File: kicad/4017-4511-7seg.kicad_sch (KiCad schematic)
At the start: 15 parts, among them U7 4017, U8 4511, U9 D168K

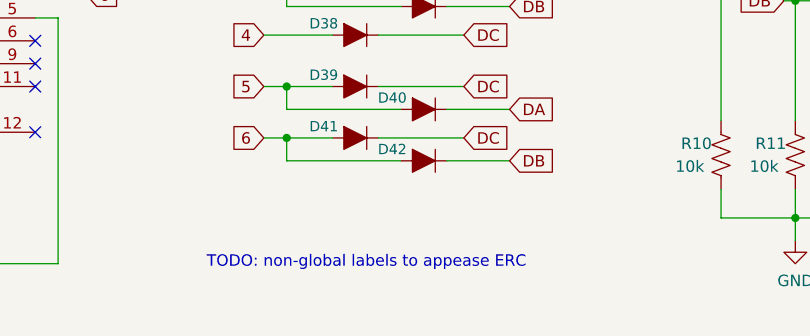
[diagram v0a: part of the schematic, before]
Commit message: Note BOM effects in different implementations
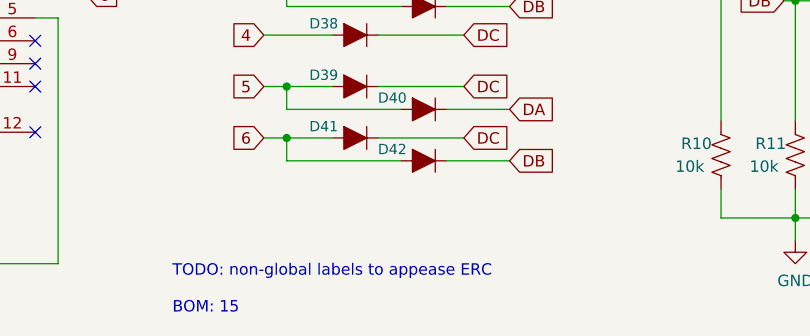
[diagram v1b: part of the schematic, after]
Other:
- note added: "TODO: non-global labels to appease ERC BOM: 15"
- note removed: "TODO: non-global labels to appease ERC"
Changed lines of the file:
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@@
     (stroke (width 0) (type default) (color 0 0 0 0))
   )
-  (text "TODO: non-global labels to appease ERC" (at 108.585 125.095 0)
+  (text "TODO: non-global labels to appease ERC\n\nBOM: 15" (at 104.775 130.175 0)
     (effects (font (size 1.27 1.27)) (justify left bottom))
   )

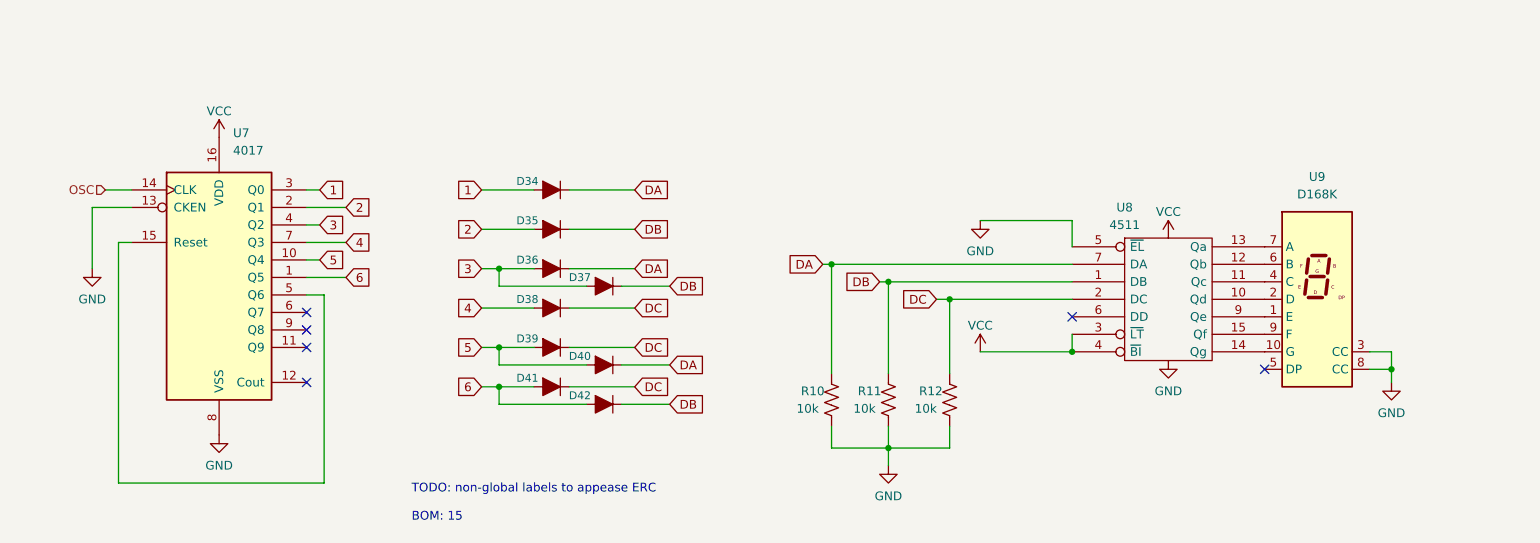
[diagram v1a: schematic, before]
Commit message: Hmmm, may need resistors for LED driver ICs
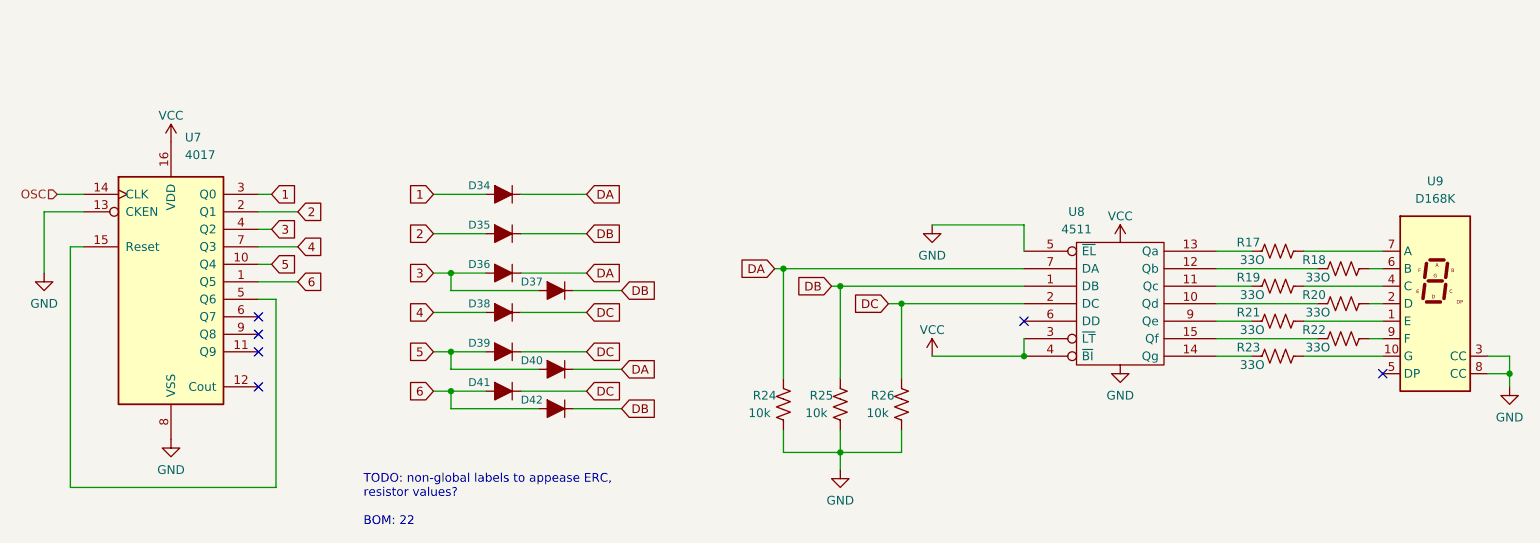
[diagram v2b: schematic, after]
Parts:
- added R17, R18, R19, R20, R21, R22, R23: 33O, Resistor_THT:R_Axial_DIN0204_L3.6mm_D1.6mm_P7.62mm_Horizontal, symbol Device:R_US
- renumbered R10 to R24, R11 to R25, R12 to R26
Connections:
- net at U8.10 (Qd): now also R20.1; no longer U9.2 (D)
- net at U8.11 (Qc): now also R19.1; no longer U9.4 (C)
- net at U8.12 (Qb): now also R18.1; no longer U9.6 (B)
- net at U8.13 (Qa): now also R17.1; no longer U9.7 (A)
- net at U8.14 (Qg): now also R23.1; no longer U9.10 (G)
- net at U8.15 (Qf): now also R22.1; no longer U9.9 (F)
- net at U8.9 (Qe): now also R21.1; no longer U9.1 (E)
- new net: R22.2, U9.9 (F)
- new net: R21.2, U9.1 (E)
- new net: R23.2, U9.10 (G)
- new net: R20.2, U9.2 (D)
- new net: R19.2, U9.4 (C)
- new net: R18.2, U9.6 (B)
- new net: R17.2, U9.7 (A)
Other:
- note added: "TODO: non-global labels to appease ERC, resistor values? BOM: 22"
- note removed: "TODO: non-global labels to appease ERC BOM: 15"
- moved on the sheet: D34, D35, D36, D37, D38, D39, D40, D41, D42, R24, R25, R26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

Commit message: TODO: fix 7seg footprint
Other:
- note added: "TODO: fix footprint! 10 A 9 B 7 C 5 D 4 E 2 F 1 G 6 DP 3 COM 8 COM"
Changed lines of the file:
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@@
     (stroke (width 0) (type default) (color 0 0 0 0))
+  )
+  (text "TODO: fix footprint!\n\n10 A\n9  B\n7  C\n5  D\n4  E\n2  F\n1  G\n\n6  DP\n3  COM\n8  COM"
+    (at 234.95 83.185 0)
+    (effects (font (size 1.27 1.27)) (justify left bottom))
   )
   (text "TODO: non-global labels to appease ERC,\nresistor values?\n\nBOM: 22"

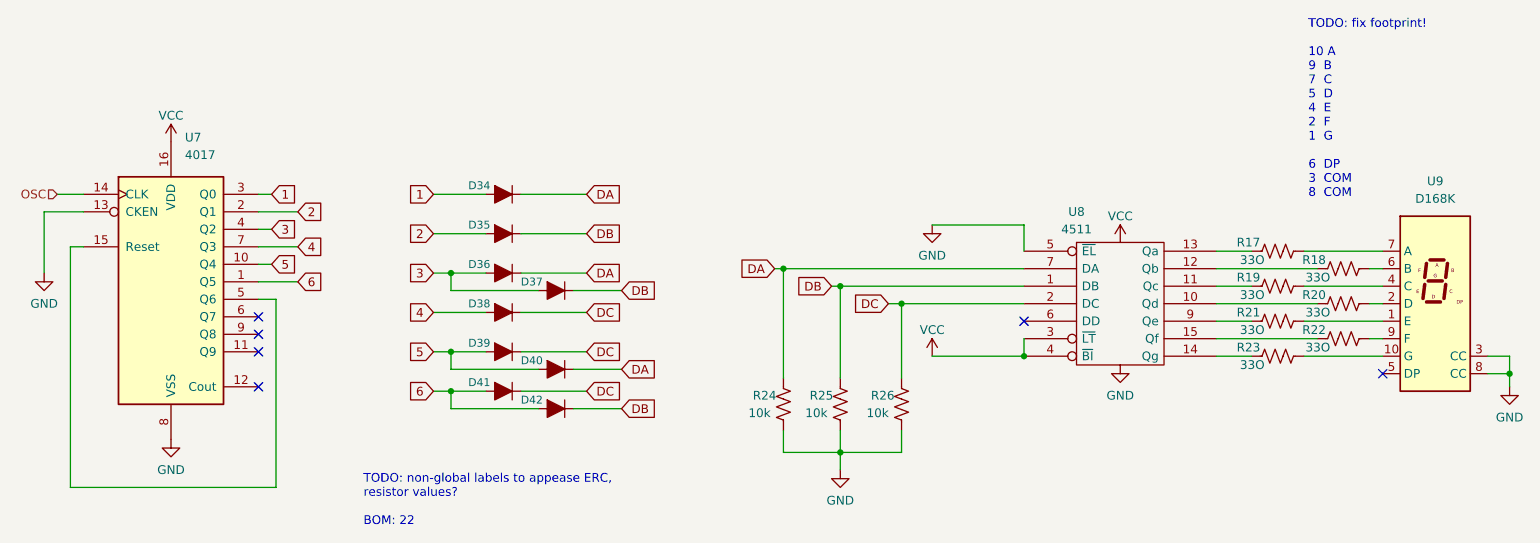
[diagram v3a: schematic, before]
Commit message: Fix 7seg footprint
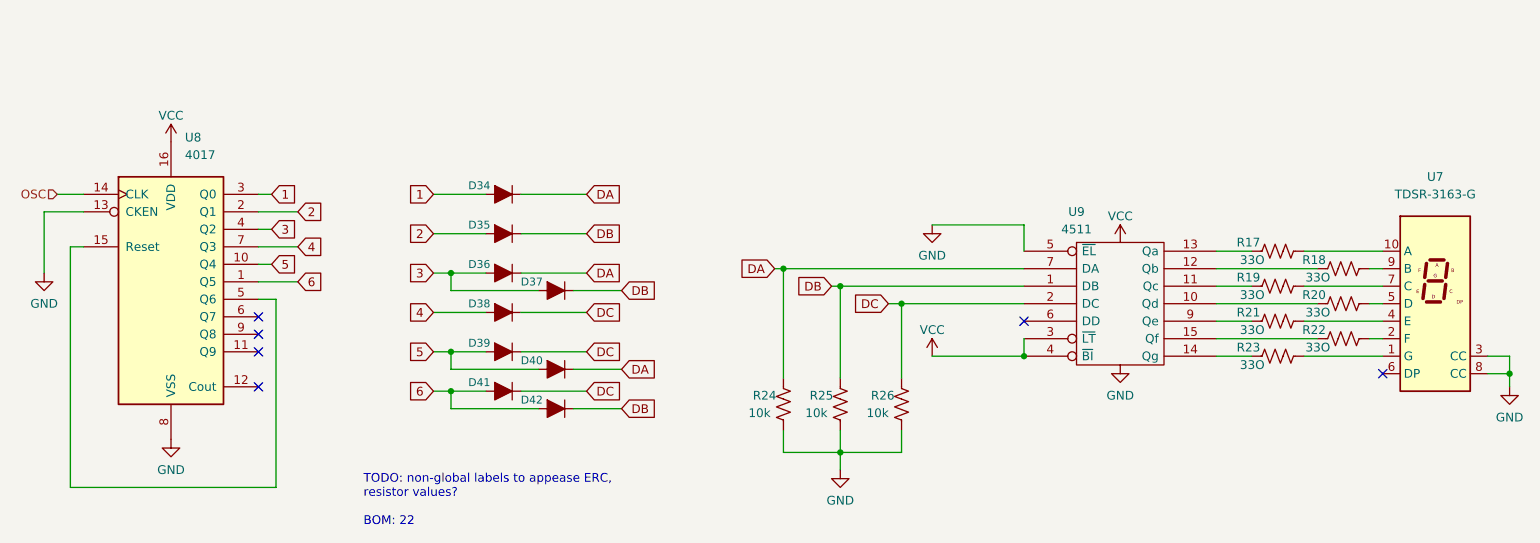
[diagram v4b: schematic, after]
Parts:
- removed U9: D168K, Display_7Segment:D1X8K, symbol Display_Character:D168K
- added U7: TDSR-3163-G, symbol parts_cafe:TDSR-3163-G
- renumbered U7 to U8, U8 to U9
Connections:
- net GND: now also U7.3 (CC), U7.8 (CC)
- net at R22.2: now also U7.2 (F)
- net at R21.2: now also U7.4 (E)
- net at R23.2: now also U7.1 (G)
- net at R20.2: now also U7.5 (D)
- net at R19.2: now also U7.7 (C)
- net at R18.2: now also U7.9 (B)
- net at R17.2: now also U7.10 (A)
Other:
- note removed: "TODO: fix footprint! 10 A 9 B 7 C 5 D 4 E 2 F 1 G 6 DP 3 COM 8 COM"

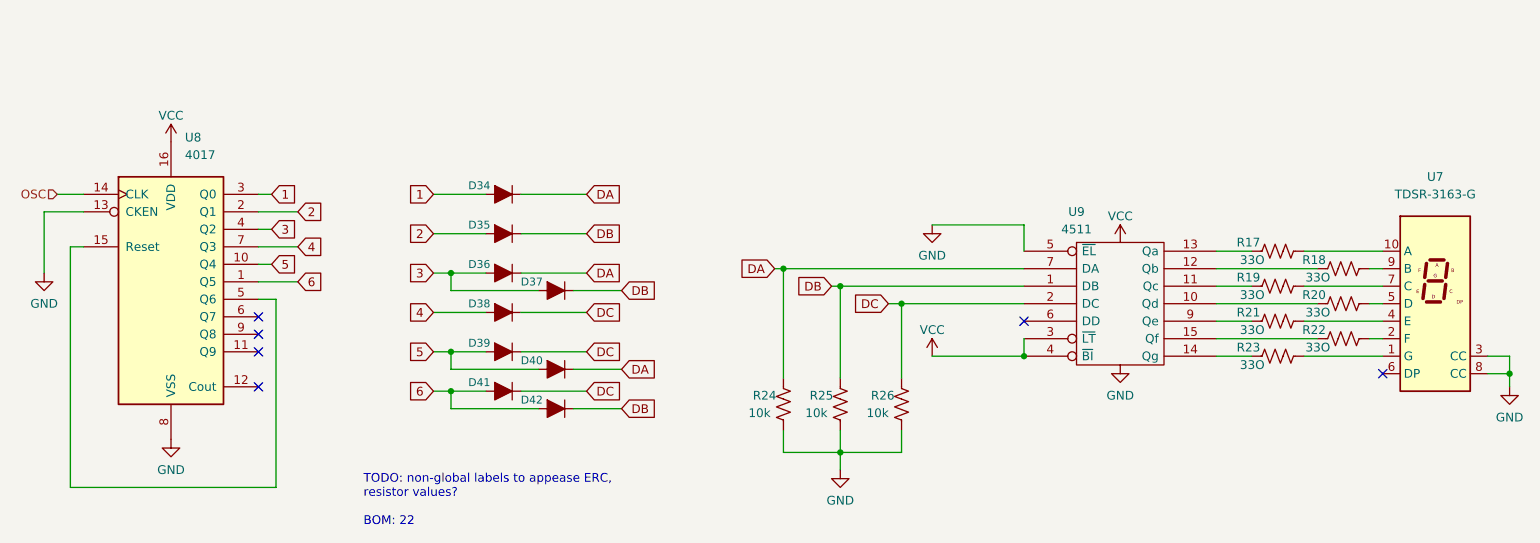
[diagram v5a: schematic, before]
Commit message: Update to latest kicad
no functional changes
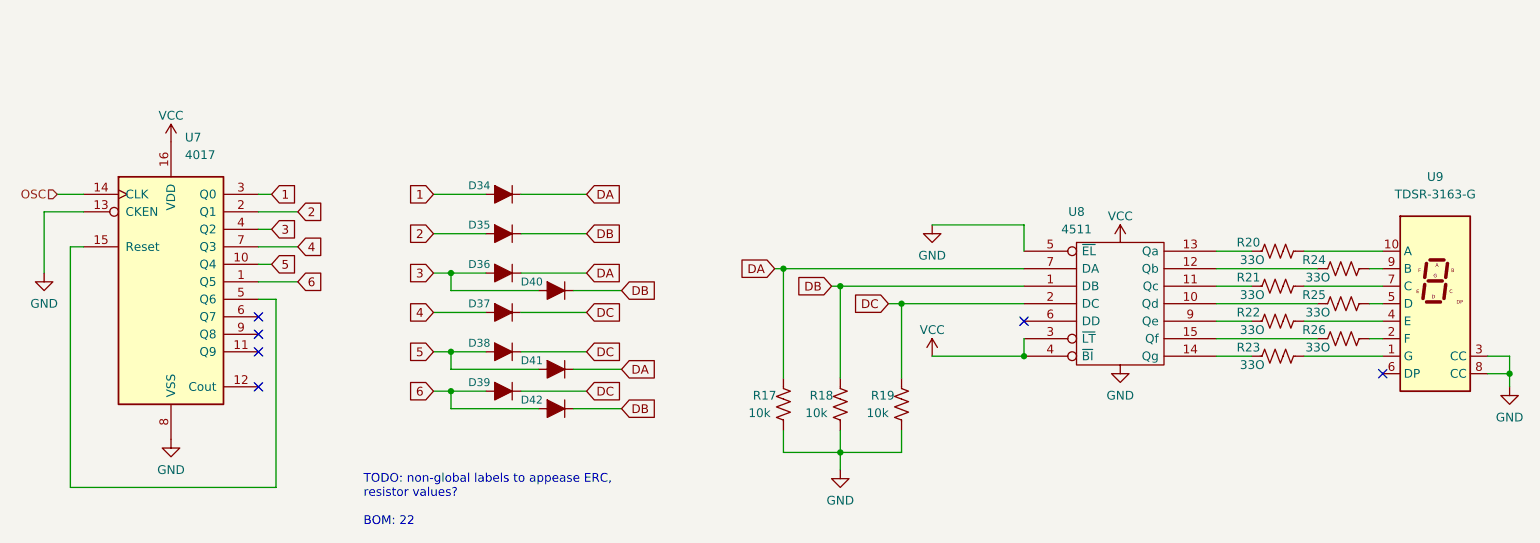
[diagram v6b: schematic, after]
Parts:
- renumbered D38 to D37, D39 to D38, D41 to D39, D37 to D40, D40 to D41, R24 to R17, R25 to R18, R26 to R19, R17 to R20, R19 to R21, R21 to R22, R18 to R24, R20 to R25, R22 to R26, U8 to U7, U9 to U8, U7 to U9
